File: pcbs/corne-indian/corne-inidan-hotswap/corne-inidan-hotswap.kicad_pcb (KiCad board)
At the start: 2 copper layers, 277.2 x 107.5 mm, 222 parts, among them J1 Conn_01x03_Pin, J2 Conn_01x04_Pin, J3 PJ-3136-B, J4 USB_A, SW1 SW_Push, SW10 SW_Push, SW11 SW_Push, SW12 SW_Push, SW13 SW_Push, SW14 SW_Push, SW15 SW_Push, SW16 SW_Push, SW17 SW_Push, SW18 SW_Push, SW19 SW_Push, SW2 SW_Push, SW20 SW_Push, SW21 SW_Push, SW3 SW_Push, SW4 SW_Push, SW5 SW_Push, SW6 SW_Push, SW7 SW_Push, SW8 SW_Push, SW9 SW_Push, U1 AP2127K-3.3, U2 RP2040, U3 W25Q32JVSS, U4 AMS1117-3.3, U5 CH334F, Y1 12Mhz

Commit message: Mid of the Component placement still the Rotarty nob is not done
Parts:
- added C18: 100nf, Capacitor_SMD:C_0603_1608Metric, F.Cu at (56.7, 207.6)
- added C19: 10uf, Capacitor_SMD:C_0805_2012Metric, F.Cu at (57.0, 211.8)
- added C20: 100nf, Capacitor_SMD:C_0603_1608Metric, F.Cu at (59.2, 207.6)
- added C21: 10uf, Capacitor_SMD:C_0805_2012Metric, F.Cu at (60.0, 211.8)
- added C22: 100nf, Capacitor_SMD:C_0603_1608Metric, F.Cu at (61.7, 207.6)
- added C23: 100nf, Capacitor_SMD:C_0603_1608Metric, F.Cu at (64.2, 207.6)
- added C24: 10uf, Capacitor_SMD:C_0805_2012Metric, F.Cu at (63.0, 211.8)
- added C25: 10uf, Capacitor_SMD:C_0805_2012Metric, F.Cu at (66.0, 211.8)
- added C26: 10uf, Capacitor_SMD:C_0805_2012Metric, F.Cu at (69.0, 211.8)
- added C27: 10uf, Capacitor_SMD:C_0805_2012Metric, F.Cu at (72.0, 211.8)
- added C28: 10uf, Capacitor_SMD:C_0805_2012Metric, F.Cu at (75.0, 211.8)
- added C29: 10uf, Capacitor_SMD:C_0805_2012Metric, F.Cu at (78.0, 211.8)
- added C30: 20pf, Capacitor_SMD:C_0603_1608Metric, F.Cu at (66.7, 207.6)
- added C31: 20pf, Capacitor_SMD:C_0603_1608Metric, F.Cu at (69.2, 207.6)
- added D2: DSK34, Diode_SMD:D_SOD-123F, F.Cu at (63.2, 169.2)
- added D3: DSK34, Diode_SMD:D_SOD-123F, F.Cu at (81.2, 211.3)
- added D4: DSK34, Diode_SMD:D_SOD-123F, F.Cu at (84.5, 211.3)
- added D5: DSK34, Diode_SMD:D_SOD-123F, F.Cu at (87.9, 211.3)
- added Q1: SI2301, Package_TO_SOT_SMD:SOT-23, F.Cu at (96.2, 211.6)
- added R10: 5K1, Resistor_SMD:R_0603_1608Metric, F.Cu at (62.2, 171.5)
- added R11: 5K1, Resistor_SMD:R_0603_1608Metric, F.Cu at (62.2, 175.2)
- added R12: 5K6, Resistor_SMD:R_0603_1608Metric, F.Cu at (64.6, 181.0)
- added R13: 10K, Resistor_SMD:R_0603_1608Metric, F.Cu at (61.1, 181.1)
- added R14: 10K, Resistor_SMD:R_0603_1608Metric, F.Cu at (71.8, 207.6)
- added R15: 0R/DNP, Resistor_SMD:R_0603_1608Metric, F.Cu at (74.3, 207.6)
- added TP4: TestPoint, TestPoint:TestPoint_Pad_D1.0mm, F.Cu at (59.8, 169.2)
- added TP7: TestPoint, TestPoint:TestPoint_Pad_D1.0mm, F.Cu at (68.0, 172.2)
- added TP8: TestPoint, TestPoint:TestPoint_Pad_D1.0mm, F.Cu at (68.0, 174.2)
- added Y2: 12Mhz, Crystal:Crystal_SMD_Abracon_ABM8AIG-4Pin_3.2x2.5mm, F.Cu at (91.8, 211.4)
- BOOT1, C1, C2, C3, C6, C8, R5, R6, rC15, rC17, rC8, rR5, rR6, rRST1: moved to B.Cu
- moved rRST1 109.6 mm to (252.5, 180.2), turned to 180 degrees
- moved BOOT1 107.9 mm to (135.0, 181.0)
- moved rR5 100.5 mm to (274.5, 155.8), turned to 90 degrees
- moved rJ1 99.9 mm to (262.5, 174.2), turned to -30 degrees
- moved J1 99.5 mm to (115.0, 174.5), turned to 30 degrees
- moved RST1 98.9 mm to (102.5, 162.5), turned to 180 degrees
- moved rBOOT1 98.2 mm to (282.5, 162.5)
- moved rR6 96.1 mm to (274.5, 152.8), turned to 90 degrees
- moved rC8 95.7 mm to (256.8, 156.2), turned to 180 degrees
- moved R6 86.4 mm to (134.2, 159.0)
- moved R5 86.4 mm to (131.0, 159.0)
- moved C8 83.7 mm to (107.2, 154.0), turned to -90 degrees
- moved rC15 47.0 mm to (221.2, 123.2), turned to 90 degrees
- moved rC17 45.1 mm to (210.2, 123.5), turned to 90 degrees
- moved C6 20.1 mm to (131.0, 157.5)
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- renumbered MCU1 to J5, J4 to J6, J4 to J7, J4 to J8
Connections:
- J4 pad 1: (no net) -> Net-(D2-K)
- J4 pad 2: (no net) -> /USB_HUB/J1_-
- J4 pad 3: (no net) -> /USB_HUB/J1_+
- J4 pad 4: (no net) -> GND
- J4 pad 5: (no net) -> GND
- J5 pad A4: VBUS -> /USB_HUB/5V
- J5 pad A5: Net-(MCU1-CC1) -> Net-(J5-CC1)
- J5 pad A6: /left/U_+ -> /USB_HUB/U_+
- J5 pad A7: /left/U_- -> /USB_HUB/U_-
- J5 pad A8: unconnected-(MCU1-SBU1-PadA8) -> unconnected-(J5-SBU1-PadA8)
- J5 pad A9: VBUS -> /USB_HUB/5V
- J5 pad B4: VBUS -> /USB_HUB/5V
- J5 pad B5: Net-(MCU1-CC2) -> Net-(J5-CC2)
- J5 pad B6: /left/U_+ -> /USB_HUB/U_+
- J5 pad B7: /left/U_- -> /USB_HUB/U_-
- J5 pad B8: unconnected-(MCU1-SBU2-PadB8) -> unconnected-(J5-SBU2-PadB8)
- J5 pad B9: VBUS -> /USB_HUB/5V
- J6 pad 1: unconnected-(J4-VBUS-Pad1) -> Net-(D3-K)
- J6 pad 2: unconnected-(J4-D--Pad2) -> /USB_HUB/J2_-
- J6 pad 3: unconnected-(J4-D+-Pad3) -> /USB_HUB/J2_+
- J6 pad 4: unconnected-(J4-GND-Pad4) -> GND
- J6 pad 5: unconnected-(J4-Shield-Pad5) -> GND
- J7 pad 1: (no net) -> Net-(D4-K)
- J7 pad 2: (no net) -> /USB_HUB/J3_-
- J7 pad 3: (no net) -> /USB_HUB/J3_+
- J7 pad 4: (no net) -> GND
- J7 pad 5: (no net) -> GND
- J8 pad 1: (no net) -> Net-(D5-K)
- J8 pad 2: (no net) -> /USB_HUB/J4_-
- J8 pad 3: (no net) -> /USB_HUB/J4_+
- J8 pad 4: (no net) -> GND
- J8 pad 5: (no net) -> GND
- U2 pad 11: unconnected-(U2-GPIO8-Pad11) -> /left/KEY_EX2
- U2 pad 13: /left/LED -> /left/L_KEY
- U2 pad 6: unconnected-(U2-GPIO4-Pad6) -> /left/KEY_EX1
- U2 pad 7: unconnected-(U2-GPIO5-Pad7) -> /left/RE0A
- U2 pad 8: unconnected-(U2-GPIO6-Pad8) -> /left/RE1A
- U2 pad 9: unconnected-(U2-GPIO7-Pad9) -> /left/REB
- U5 pad 10: unconnected-(U5-DP2+-Pad10) -> /USB_HUB/J2_+
- U5 pad 11: unconnected-(U5-DM1--Pad11) -> /USB_HUB/J1_-
- U5 pad 12: unconnected-(U5-DP1+-Pad12) -> /USB_HUB/J1_+
- U5 pad 14: unconnected-(U5-DMU--Pad14) -> /USB_HUB/U_-
- U5 pad 15: unconnected-(U5-DPU+-Pad15) -> /USB_HUB/U_+
- U5 pad 19: unconnected-(U5-V5-Pad19) -> H+5V
- U5 pad 20: unconnected-(U5-VDD33_{LDO}-Pad20) -> H+3.3V
- U5 pad 25: unconnected-(U5-GND-Pad25) -> GND
- U5 pad 3: unconnected-(U5-XO-Pad3) -> Net-(U5-XO)
- U5 pad 4: unconnected-(U5-XI-Pad4) -> Net-(U5-XI)
- U5 pad 5: unconnected-(U5-DM4--Pad5) -> /USB_HUB/J4_-
- U5 pad 6: unconnected-(U5-DP4+-Pad6) -> /USB_HUB/J4_+
- U5 pad 7: unconnected-(U5-DM3--Pad7) -> /USB_HUB/J3_-
- U5 pad 8: unconnected-(U5-DP3+-Pad8) -> /USB_HUB/J3_+
- U5 pad 9: unconnected-(U5-DM2--Pad9) -> /USB_HUB/J2_-
- rU2 pad 11: unconnected-(rU2-GPIO8-Pad11) -> /Right/KEY_19
- rU2 pad 12: /Right/KEY_2 -> /Right/KEY_18
- rU2 pad 13: /Right/LED -> /Right/L_KEY
- rU2 pad 14: /Right/KEY_1 -> /Right/KEY_20
- rU2 pad 17: /Right/KEY_9 -> /Right/KEY_17
- rU2 pad 18: /Right/KEY_8 -> /Right/KEY_21
- rU2 pad 2: /Right/KEY_4 -> /Right/KEY_11
- rU2 pad 27: /Right/KEY_16 -> /Right/KEY_9
- rU2 pad 28: /Right/KEY_21 -> /Right/KEY_8
- rU2 pad 29: /Right/KEY_17 -> /Right/KEY_16
- rU2 pad 3: /Right/KEY_6 -> /Right/KEY_5
- rU2 pad 30: /Right/KEY_20 -> /Right/KEY_1
- rU2 pad 31: /Right/KEY_18 -> /Right/KEY_7
- rU2 pad 34: /Right/KEY_19 -> /Right/KEY_2
- rU2 pad 35: /Right/KEY_13 -> /Right/KEY_EX2
- rU2 pad 36: /Right/KEY_14 -> /Right/RE0A
- rU2 pad 37: /Right/KEY_15 -> /Right/KEY_EX1
- rU2 pad 38: /Right/KEY_12 -> /Right/KEY_3
- rU2 pad 39: /Right/KEY_11 -> /Right/KEY_4
- rU2 pad 4: /Right/KEY_3 -> /Right/KEY_12
- rU2 pad 40: /Right/KEY_10 -> /Right/KEY_6
- rU2 pad 41: /Right/KEY_5 -> /Right/KEY_10
- rU2 pad 5: /Right/KEY_7 -> /Right/KEY_13
- rU2 pad 6: unconnected-(rU2-GPIO4-Pad6) -> /Right/KEY_14
- rU2 pad 7: unconnected-(rU2-GPIO5-Pad7) -> /Right/KEY_15
- rU2 pad 8: unconnected-(rU2-GPIO6-Pad8) -> /Right/RE1A
- rU2 pad 9: unconnected-(rU2-GPIO7-Pad9) -> /Right/REB
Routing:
- net +3.3V: track 33.2 -> 87.4 mm, vias 0 -> 5
- net /left/L_KEY: track 0.00 -> 44.9 mm
- net /left/KEY_1: track 0.00 -> 44.5 mm
- net /left/KEY_2: track 0.00 -> 31.9 mm
- net /Right/KEY_1: track 0.00 -> 12.8 mm
- net Net-(U2-VREG_VOUT): track 0.00 -> 8.47 mm
- net /left/D-: track 0.00 -> 5.00 mm
- net /left/D+: track 0.00 -> 4.98 mm
- net /Right/KEY_3: track 0.00 -> 4.08 mm
- net /Right/KEY_6: track 0.00 -> 3.97 mm
- net /Right/KEY_10: track 0.00 -> 3.90 mm
- net /Right/KEY_4: track 0.00 -> 3.66 mm
- net /left/KEY_6: track 0.00 -> 3.29 mm
- net /left/RESET: track 0.00 -> 3.25 mm
- net /left/KEY_4: track 0.00 -> 3.25 mm
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
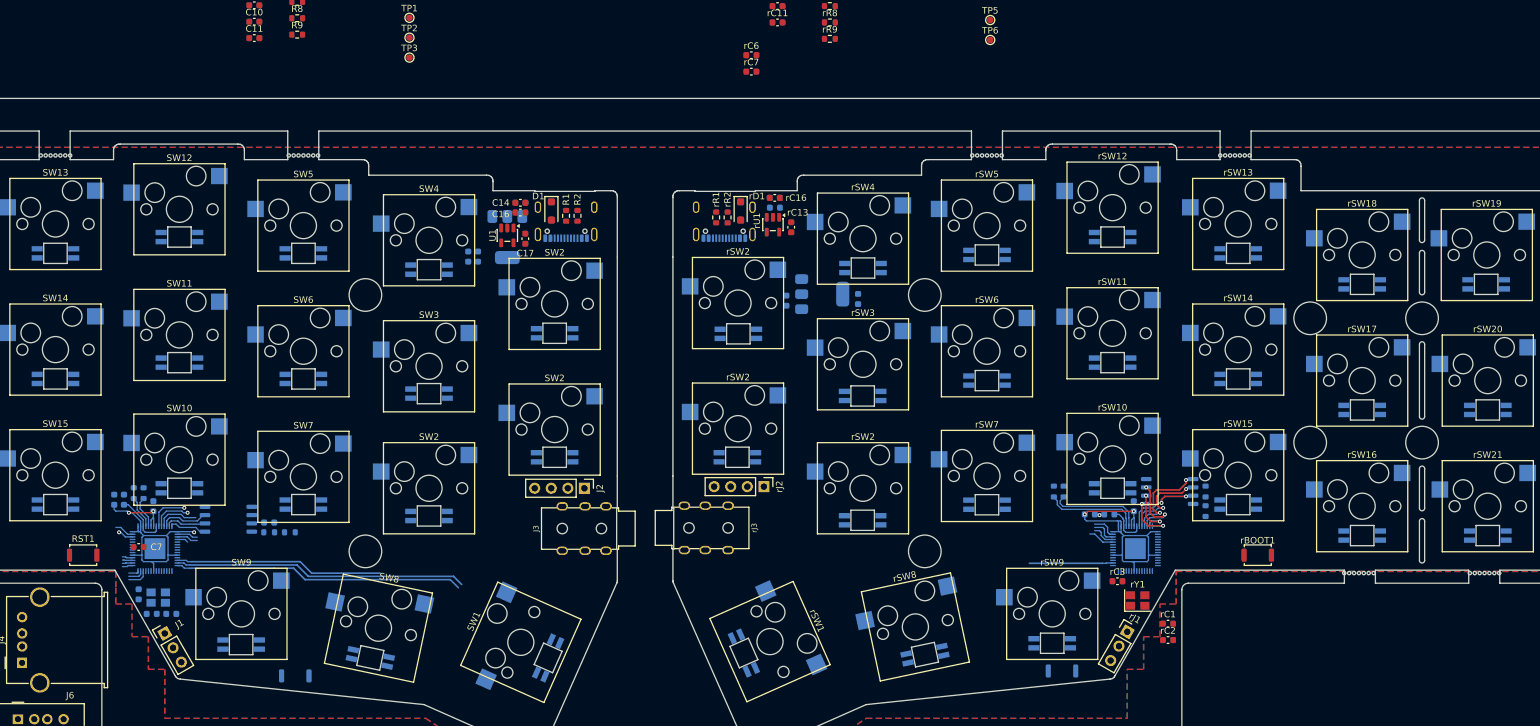
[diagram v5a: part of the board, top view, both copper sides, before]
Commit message: Rotart encode also added in PCB layout
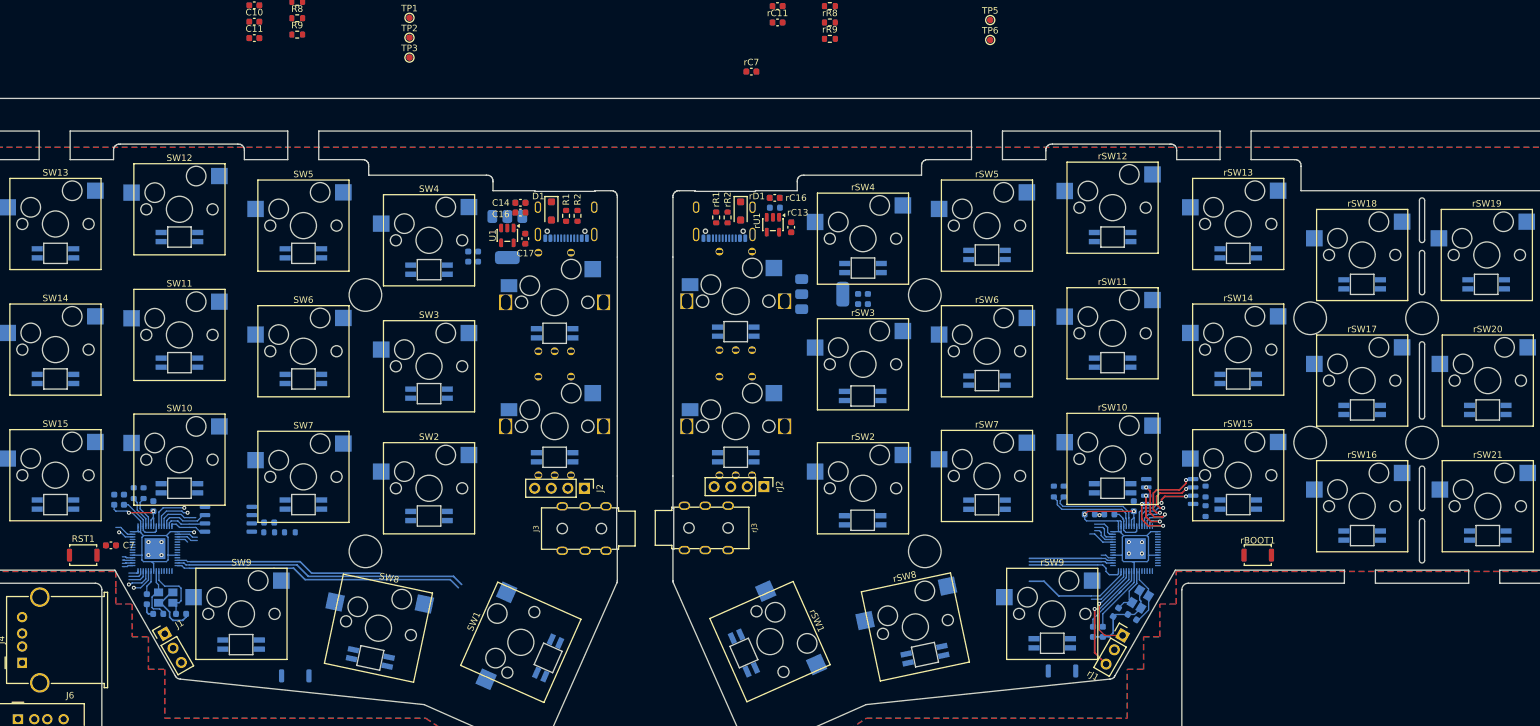
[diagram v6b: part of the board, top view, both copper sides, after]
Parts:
- removed ? (x42): , 
- removed the SW2 at (174.8, 143.2)
- removed the SW2 at (174.8, 124.0)
- removed the rSW2 at (202.8, 143.1)
- removed the rSW2 at (202.8, 123.9)
- added EXSW1: RotaryEncoder_Switch, User_Button_Switch_Keyboard:keyswitch_cherrymx_hotswap_1u_rotary_encoder_ec12, B.Cu at (174.8, 123.8)
- added EXSW2: RotaryEncoder_Switch, User_Button_Switch_Keyboard:keyswitch_cherrymx_hotswap_1u_rotary_encoder_ec12, B.Cu at (174.8, 142.8)
- added rEXSW1: RotaryEncoder_Switch, User_Button_Switch_Keyboard:keyswitch_cherrymx_hotswap_1u_rotary_encoder_ec12, B.Cu at (202.5, 123.6)
- added rEXSW2: RotaryEncoder_Switch, User_Button_Switch_Keyboard:keyswitch_cherrymx_hotswap_1u_rotary_encoder_ec12, B.Cu at (202.5, 142.8)
- EXLED1, EXLED2, rEXLED1, rEXLED2: value YS-SK6812MINI-E -> SK6812MINI-E; footprint kbd_local:YS-SK6812MINI-E -> User_Button_Switch_Keyboard:YS-SK6812MINI-E
- rC1, rC2, rC3, rC6, rY1: moved to B.Cu
- moved rC6 103.5 mm to (258.8, 174.2), turned to 90 degrees
- moved rC17 12.5 mm to (222.8, 123.2)
- moved rC2 9.06 mm to (260.8, 171.2), turned to 58 degrees
- moved rC3 8.61 mm to (257.2, 174.2), turned to 90 degrees
- moved rC1 5.59 mm to (263.2, 172.0), turned to -32 degrees
- moved C7 4.26 mm to (106.8, 161.0)
- moved C1 1.50 mm to (117.5, 171.5)
- moved C3 1.46 mm to (112.2, 169.2)
- moved Y1 1.15 mm to (115.2, 169.0)
- moved C2 1.00 mm to (114.0, 171.5)
- moved rJ1 0.90 mm to (261.8, 174.8)
- moved rEXLED1 0.52 mm to (202.5, 128.2)
- moved rY1 0.45 mm to (264.5, 169.2), turned to 58 degrees
- moved rEXLED2 0.25 mm to (202.5, 147.5)
- moved J1 0.05 mm to (115.0, 174.6)
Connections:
- net Net-(EXLED1-DOUT) renamed /left/L_KEY23
- net Net-(rEXLED1-DOUT) renamed /Right/L_KEY23
- EXLED1 pad 1: Net-(D1-K) -> /left/5V_L
- EXLED1 pad 4: Net-(EXLED1-DIN) -> /left/L_KEY22
- EXLED2 pad 1: Net-(D1-K) -> /left/5V_L
- rEXLED1 pad 1: Net-(rD1-K) -> /Right/5V_L
- rEXLED1 pad 3: GNDR -> GND
- rEXLED1 pad 4: Net-(rEXLED1-DIN) -> /Right/L_KEY22
- rEXLED2 pad 1: Net-(rD1-K) -> /Right/5V_L
- rEXLED2 pad 3: GNDR -> GND
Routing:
- net GND: track 1.58 -> 26.9 mm, vias 13 -> 21
- net /Right/SWCLK: track 0.00 -> 17.6 mm, vias 0 -> 1
- net /Right/KEY_9: track 0.00 -> 16.9 mm
- net /Right/KEY_8: track 0.00 -> 15.0 mm
- net /Right/SWDIO: track 0.00 -> 14.8 mm, vias 0 -> 1
- net /Right/KEY_7: track 0.00 -> 12.9 mm
- net Net-(rU2-VREG_VOUT): track 6.43 -> 17.8 mm
- net Net-(U2-XIN): track 0.00 -> 11.0 mm
- net +3.3V: track 87.4 -> 97.9 mm
- net Net-(rU2-XIN): track 0.00 -> 9.04 mm
- net Net-(U2-XOUT): track 0.00 -> 8.67 mm
- net Net-(rU2-XOUT): track 0.00 -> 7.90 mm
- net /Right/RESET: track 0.00 -> 7.24 mm
- net /left/SWDIO: track 0.00 -> 4.16 mm, vias 0 -> 1
- net /left/SWCLK: track 0.00 -> 4.11 mm, vias 0 -> 1
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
